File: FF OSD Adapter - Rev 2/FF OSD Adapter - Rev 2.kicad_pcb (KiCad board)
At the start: 2 copper layers, 78.7 x 24.1 mm, 10 parts, among them CN1 Conn_01x09, CN2 Conn_01x09, CN3 Conn_01x04, CN4 Conn_01x04, U1 YAAJ_BluePill_Part_Like

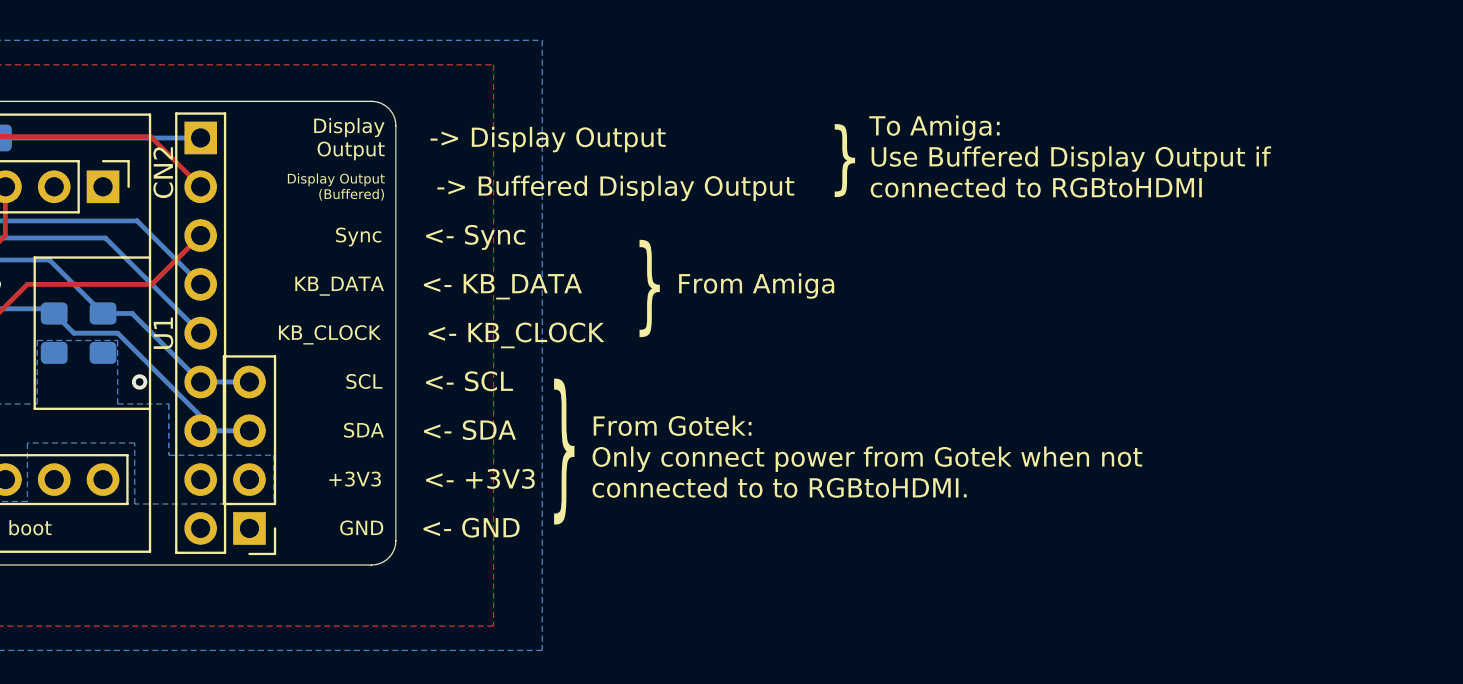
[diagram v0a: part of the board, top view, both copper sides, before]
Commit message: Updated schematic and board to show the I2C display pins better
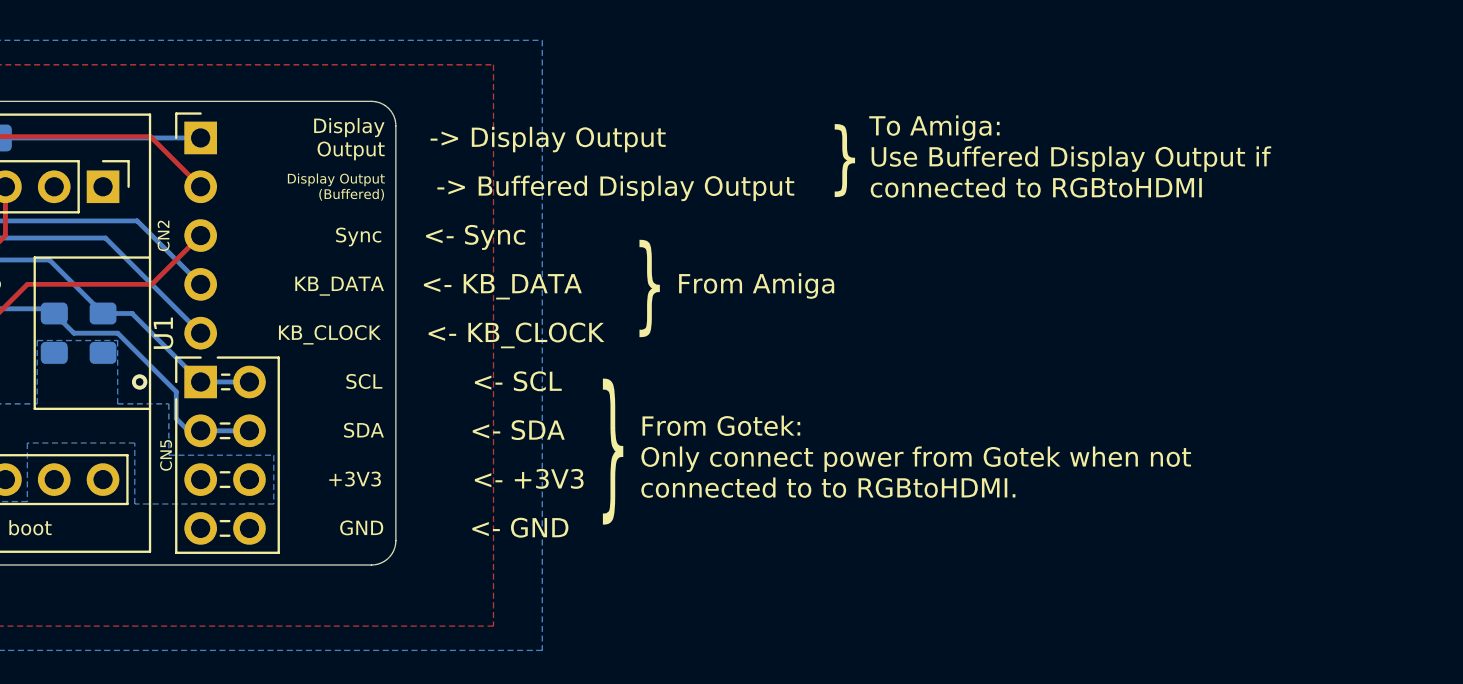
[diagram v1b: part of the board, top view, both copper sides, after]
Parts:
- removed CN4: Conn_01x04, Connector_PinHeader_2.54mm:PinHeader_1x04_P2.54mm_Vertical
- added CN5: Conn_02x04_Row_Letter_First, Connector_PinHeader_2.54mm:PinHeader_2x04_P2.54mm_Horizontal, F.Cu at (175.3, 104.1)
- CN2: value Conn_01x09 -> Conn_01x05; footprint Connector_PinHeader_2.54mm:PinHeader_1x09_P2.54mm_Horizontal -> Connector_PinHeader_2.54mm:PinHeader_1x05_P2.54mm_Horizontal
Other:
- board text added: "Serial"
